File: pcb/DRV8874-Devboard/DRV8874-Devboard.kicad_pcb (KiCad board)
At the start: 4 copper layers, 65 x 67 mm, 40 parts, among them J1 Conn_01x04_Pin, J2 Screw_Terminal_01x02, J3 Conn_01x03_Pin, J4 Conn_01x03_Pin, J5 Conn_01x04_Pin, J6 Conn_01x03_Pin, J7 Conn_01x03_Pin, J8 Conn_01x04_Pin, J9 Conn_01x03_Pin, U1 DRV8874, U2 BL9342, U4 SN65HVD230, U5 TPS16630PWPR, U7 TinyThinker_J1

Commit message: started working on CAN
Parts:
- moved U4 34.4 mm to (141.0, 92.5), turned to -90 degrees
- moved R3 27.5 mm to (141.5, 98.5)
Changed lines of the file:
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@@
 	(footprint "Resistor_SMD:R_0402_1005Metric"
 		(layer "F.Cu")
-		(at 164.03 82.8)
+		(at 141.5 98.5)
 		(descr "Resistor SMD 0402 (1005 Metric), square (rectangular) end terminal, IPC-7351 nominal, (Body size source: IPC-SM-782 page 72, https://www.pcb-3d.com/wordpress/wp-content/uploads/ipc-sm-782a_amendment_1_and_2.pdf), generated with kicad-footprint-generator")
 		(tags "resistor")
@@
 	(footprint "Package_SO:SOIC-8_3.9x4.9mm_P1.27mm"
 		(layer "F.Cu")
-		(at 163.15 66.135)
+		(at 141 92.5 -90)
 		(descr "SOIC, 8 Pin (JEDEC MS-012AA, https://www.analog.com/media/en/package-pcb-resources/package/pkg_pdf/soic_narrow-r/r_8.pdf), generated with kicad-footprint-generator ipc_gullwing_generator.py")
 		(tags "SOIC SO")
 		(property "Reference" "U4"
-			(at 0 -3.4 0)
+			(at 0 -4 90)
 			(layer "F.SilkS")
 			(effects
@@
 		)
 		(property "Value" "SN65HVD230"
-			(at 0 3.4 0)
+			(at 0 3.4 90)
 			(layer "F.Fab")
 			(effects
@@
 		)
 		(property "Datasheet" "http://www.ti.com/lit/ds/symlink/sn65hvd230.pdf"
-			(at 0 0 0)
+			(at 0 0 90)
 			(layer "F.Fab")
 			(hide yes)
@@
 		)
 		(property "Description" "CAN Bus Transceivers, 3.3V, 1Mbps, Low-Power capabilities, SOIC-8"
-			(at 0 0 0)
+			(at 0 0 90)
 			(layer "F.Fab")
 			(hide yes)
@@
 		)
 		(property "Sim.Device" ""
-			(at 0 0 0)
+			(at 0 0 270)
 			(unlocked yes)
 			(layer "F.Fab")
@@
 		)
 		(property "Sim.Pins" ""
-			(at 0 0 0)
+			(at 0 0 270)
 			(unlocked yes)
 			(layer "F.Fab")
@@
 		)
 		(property "Sim.Type" ""
-			(at 0 0 0)
+			(at 0 0 270)
 			(unlocked yes)
 			(layer "F.Fab")
@@
 		(attr smd)
 		(fp_line
-			(start -2.06 -2.56)
-			(end 2.06 -2.56)
+			(start -2.06 2.56)
+			(end -2.06 2.465)
 			(stroke
 				(width 0.12)
@@
 		)
 		(fp_line
-			(start -2.06 -2.465)
-			(end -2.06 -2.56)
+			(start 2.06 2.56)
+			(end -2.06 2.56)
 			(stroke
 				(width 0.12)
@@
 		)
 		(fp_line
-			(start -2.06 2.56)
-			(end -2.06 2.465)
+			(start 2.06 2.465)
+			(end 2.06 2.56)
 			(stroke
 				(width 0.12)
@@
 		)
 		(fp_line
-			(start 2.06 -2.56)
-			(end 2.06 -2.465)
+			(start -2.06 -2.465)
+			(end -2.06 -2.56)
 			(stroke
 				(width 0.12)
@@
 		)
 		(fp_line
-			(start 2.06 2.465)
-			(end 2.06 2.56)
+			(start -2.06 -2.56)
+			(end 2.06 -2.56)
 			(stroke
 				(width 0.12)
@@
 		)
 		(fp_line
-			(start 2.06 2.56)
-			(end -2.06 2.56)
+			(start 2.06 -2.56)
+			(end 2.06 -2.465)
 			(stroke
 				(width 0.12)
@@
 		)
 		(fp_line
-			(start -3.7 -2.46)
-			(end -2.2 -2.46)
+			(start -2.2 2.7)
+			(end -2.2 2.46)
 			(stroke
 				(width 0.05)
@@
 		)
 		(fp_line
-			(start -3.7 2.46)
-			(end -3.7 -2.46)
+			(start 2.2 2.7)
+			(end -2.2 2.7)
 			(stroke
 				(width 0.05)
@@
 		)
 		(fp_line
-			(start -2.2 -2.7)
-			(end 2.2 -2.7)
+			(start -3.7 2.46)
+			(end -3.7 -2.46)
 			(stroke
 				(width 0.05)
@@
 		)
 		(fp_line
-			(start -2.2 -2.46)
-			(end -2.2 -2.7)
+			(start -2.2 2.46)
+			(end -3.7 2.46)
 			(stroke
 				(width 0.05)
@@
 		)
 		(fp_line
-			(start -2.2 2.46)
-			(end -3.7 2.46)
+			(start 2.2 2.46)
+			(end 2.2 2.7)
 			(stroke
 				(width 0.05)
@@
 		)
 		(fp_line
-			(start -2.2 2.7)
-			(end -2.2 2.46)
+			(start 3.7 2.46)
+			(end 2.2 2.46)
 			(stroke
 				(width 0.05)
@@
 		)
 		(fp_line
-			(start 2.2 -2.7)
-			(end 2.2 -2.46)
+			(start -3.7 -2.46)
+			(end -2.2 -2.46)
 			(stroke
 				(width 0.05)
@@
 		)
 		(fp_line
-			(start 2.2 -2.46)
-			(end 3.7 -2.46)
+			(start -2.2 -2.46)
+			(end -2.2 -2.7)
 			(stroke
 				(width 0.05)
@@
 		)
 		(fp_line
-			(start 2.2 2.46)
-			(end 2.2 2.7)
+			(start 2.2 -2.46)
+			(end 3.7 -2.46)
 			(stroke
 				(width 0.05)
@@
 		)
 		(fp_line
-			(start 2.2 2.7)
-			(end -2.2 2.7)
+			(start 3.7 -2.46)
+			(end 3.7 2.46)
 			(stroke
 				(width 0.05)
@@
 		)
 		(fp_line
-			(start 3.7 -2.46)
-			(end 3.7 2.46)
+			(start -2.2 -2.7)
+			(end 2.2 -2.7)
 			(stroke
 				(width 0.05)
@@
 		)
 		(fp_line
-			(start 3.7 2.46)
-			(end 2.2 2.46)
+			(start 2.2 -2.7)
+			(end 2.2 -2.46)
 			(stroke
 				(width 0.05)
@@
 		)
 		(fp_text user "${REFERENCE}"
-			(at 0 0 90)
+			(at 0 0 0)
 			(layer "F.Fab")
 			(effects
@@
 		)
 		(pad "1" smd roundrect
-			(at -2.475 -1.905)
+			(at -2.475 -1.905 270)
 			(size 1.95 0.6)
 			(layers "F.Cu" "F.Mask" "F.Paste")
@@
 		)
 		(pad "2" smd roundrect
-			(at -2.475 -0.635)
+			(at -2.475 -0.635 270)
 			(size 1.95 0.6)
 			(layers "F.Cu" "F.Mask" "F.Paste")
@@
 		)
 		(pad "3" smd roundrect
-			(at -2.475 0.635)
+			(at -2.475 0.635 270)
 			(size 1.95 0.6)
 			(layers "F.Cu" "F.Mask" "F.Paste")
@@
 		)
 		(pad "4" smd roundrect
-			(at -2.475 1.905)
+			(at -2.475 1.905 270)
 			(size 1.95 0.6)
 			(layers "F.Cu" "F.Mask" "F.Paste")
@@
 		)
 		(pad "5" smd roundrect
-			(at 2.475 1.905)
+			(at 2.475 1.905 270)
 			(size 1.95 0.6)
 			(layers "F.Cu" "F.Mask" "F.Paste")
@@
 		)
 		(pad "6" smd roundrect
-			(at 2.475 0.635)
+			(at 2.475 0.635 270)
 			(size 1.95 0.6)
 			(layers "F.Cu" "F.Mask" "F.Paste")
@@
 		)
 		(pad "7" smd roundrect
-			(at 2.475 -0.635)
+			(at 2.475 -0.635 270)
 			(size 1.95 0.6)
 			(layers "F.Cu" "F.Mask" "F.Paste")
@@
 		)
 		(pad "8" smd roundrect
-			(at 2.475 -1.905)
+			(at 2.475 -1.905 270)
 			(size 1.95 0.6)
 			(layers "F.Cu" "F.Mask" "F.Paste")

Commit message: Started working on layout
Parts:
- added C6: 330uF, Capacitor_SMD:CP_Elec_10x10.5, F.Cu at (187.2, 81.4)
- added C7: 22nF, Capacitor_SMD:C_0603_1608Metric, F.Cu at (181.8, 88.7)
- added C8: 100nF, Capacitor_SMD:C_0402_1005Metric, F.Cu at (195.8, 76.3)
- added C9: 100nF, Capacitor_SMD:C_0402_1005Metric, F.Cu at (195.8, 78.3)
- added J10: Conn_01x06_Pin, Connector_PinHeader_2.54mm:PinHeader_1x06_P2.54mm_Vertical, F.Cu at (109.0, 70.7)
- added J11: Conn_01x04_Pin, Connector_PinHeader_2.54mm:PinHeader_1x04_P2.54mm_Vertical, F.Cu at (177.5, 77.7)
- added J12: Conn_01x03_Pin, Connector_PinHeader_2.54mm:PinHeader_1x03_P2.54mm_Vertical, F.Cu at (186.1, 89.7)
- added R16: 15k, Resistor_SMD:R_0603_1608Metric, F.Cu at (181.8, 91.2)
- added R17: 75k, Resistor_SMD:R_0603_1608Metric, F.Cu at (181.8, 93.7)
- added R18: 20k, Resistor_SMD:R_0603_1608Metric, F.Cu at (181.8, 96.2)
- added R19: 2k2, Resistor_SMD:R_0402_1005Metric, F.Cu at (194.2, 95.0)
- added R20: 10k, Resistor_SMD:R_0805_2012Metric, F.Cu at (190.6, 95.5)
- added U3: DRV8874, Package_SO:HTSSOP-16-1EP_4.4x5mm_P0.65mm_EP3.4x5mm_Mask2.46x2.31mm, F.Cu at (135.1, 72.5)
- R10, R7: footprint PCM_JLCPCB:R_0603 -> Resistor_SMD:R_0603_1608Metric
- U1: footprint Package_SO:HTSSOP-16-1EP_4.4x5mm_P0.65mm_EP3.4x5mm_Mask2.66x2.46mm -> Package_SO:HTSSOP-16-1EP_4.4x5mm_P0.65mm_EP3.4x5mm_Mask2.46x2.31mm
- U7: moved to B.Cu
- moved J9 70.9 mm to (125.0, 51.5), turned to -90 degrees
- moved J8 66.1 mm to (127.6, 47.5), turned to -90 degrees
- moved R2 65.8 mm to (122.0, 93.5)
- moved R15 65.7 mm to (128.0, 52.0), turned to -90 degrees
- moved C1 55.1 mm to (133.2, 53.3), turned to 180 degrees
- moved R13 54.7 mm to (130.0, 57.8), turned to -90 degrees
- moved R14 53.8 mm to (130.0, 61.3), turned to -90 degrees
- moved U5 52.9 mm to (136.5, 97.5), turned to 90 degrees
- moved C13 52.6 mm to (187.5, 109.2), turned to 90 degrees
- moved J7 50.2 mm to (111.5, 104.5), turned to 90 degrees
- moved R6 49.4 mm to (137.0, 89.5), turned to -90 degrees
- moved R11 46.7 mm to (185.5, 109.2), turned to -90 degrees
- moved J6 43.1 mm to (121.0, 85.4)
- moved J4 42.8 mm to (111.4, 96.5), turned to 90 degrees
- moved R12 42.4 mm to (185.5, 112.7), turned to 90 degrees
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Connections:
- net /BL9342_EN renamed /BL_EN
- net /PMODE_A renamed /A_PMODE
- net Net-(D2-K) renamed /BL_SW
- net Net-(J4-Pin_2) renamed /CAN_TERM
- net Net-(J6-Pin_2) renamed /CAN_RS
- net Net-(J6-Pin_3) renamed /CAN_RS_R
- net Net-(J9-Pin_1) renamed /A_IMODE_R
- net Net-(J9-Pin_2) renamed /A_IMODE
- net Net-(U1-CPH) renamed /A_CPH
- net Net-(U1-CPL) renamed /A_CPL
- net Net-(U1-VCP) renamed /A_VCP
- net Net-(U1-VREF) renamed /A_VREF
- net Net-(U1-nFAULT) renamed /A_nFault
- net Net-(U2-BST) renamed /BL_BST
- net Net-(U2-FB) renamed /BL_FB
- net Net-(U5-*FLT) renamed /TPS_FLT
- net Net-(U5-DVDT) renamed /TPS_DVDT
- net Net-(U5-ILIM) renamed /TPS_ILIM
- net Net-(U5-IMON) renamed /TPS_MON
- net Net-(U5-OVP) renamed /TPS_OVP
- net Net-(U5-UVLO) renamed /TPS_UVLO
- C12 pad 1: Net-(U2-VIN) -> +BATT_PROT
- R1 pad 1: Net-(U1-IPROPI) -> /A_IPROPI
- U1 pad 1: unconnected-(U1-EN/IN1-Pad1) -> /A_IN1
- U1 pad 10: /Phase_A- -> /A_OUT-
- U1 pad 2: unconnected-(U1-PH/IN2-Pad2) -> /A_IN2
- U1 pad 6: Net-(U1-IPROPI) -> /A_IPROPI
- U1 pad 8: /Phase_A+ -> /A_OUT+
- U2 pad 5: Net-(U2-VIN) -> +BATT_PROT
- U7 pad 1: unconnected-(U7A-+5V_EXT-Pad1) -> +5V
- U7 pad 10: unconnected-(U7A-GND-Pad10) -> GND
- U7 pad 11: unconnected-(U7A-GND-Pad11) -> GND
- U7 pad 13: unconnected-(U7A-+3.3V-Pad13) -> +3.3V
- U7 pad 14: unconnected-(U7A-GND-Pad14) -> GND
- U7 pad 15: unconnected-(U7A-GND-Pad15) -> GND
- U7 pad 16: unconnected-(U7A-+3.3V-Pad16) -> +3.3V
- U7 pad 17: unconnected-(U7A-ADC1_IN9-Pad17) -> /A_IPROPI
- U7 pad 18: unconnected-(U7A-GND-Pad18) -> GND
- U7 pad 19: unconnected-(U7A-GND-Pad19) -> GND
- U7 pad 2: unconnected-(U7A-GND-Pad2) -> GND
- U7 pad 21: unconnected-(U7A-ADC1_IN15-Pad21) -> /B_IPROPI
- U7 pad 22: unconnected-(U7A-GND-Pad22) -> GND
- U7 pad 23: unconnected-(U7A-GND-Pad23) -> GND
- U7 pad 25: unconnected-(U7A-+3.3V-Pad25) -> +3.3V
- U7 pad 26: unconnected-(U7A-GND-Pad26) -> GND
- U7 pad 27: unconnected-(U7A-GND-Pad27) -> GND
- U7 pad 28: unconnected-(U7A-+3.3V-Pad28) -> +3.3V
- U7 pad 30: unconnected-(U7A-GND-Pad30) -> GND
- U7 pad 31: unconnected-(U7A-GND-Pad31) -> GND
- U7 pad 34: unconnected-(U7A-GND-Pad34) -> GND
- U7 pad 35: unconnected-(U7A-GND-Pad35) -> GND
- U7 pad 37: unconnected-(U7A-+3.3V-Pad37) -> +3.3V
- U7 pad 38: unconnected-(U7A-GND-Pad38) -> GND
- U7 pad 39: unconnected-(U7A-GND-Pad39) -> GND
- U7 pad 4: unconnected-(U7A-GND-Pad4) -> GND
- U7 pad 51: unconnected-(U7B-SPI1_NSS-Pad51) -> /SPI1_NSS
- U7 pad 53: unconnected-(U7B-SPI1_SCK-Pad53) -> /SPI1_SCK
- U7 pad 55: unconnected-(U7B-SPI1_MISO-Pad55) -> /SPI1_MISO
- U7 pad 57: unconnected-(U7B-SPI1_MOSI-Pad57) -> /SPI1_MOSI
- U7 pad 6: unconnected-(U7A-GND-Pad6) -> GND
- U7 pad 7: unconnected-(U7A-GND-Pad7) -> GND
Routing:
- net /CAN1_TX: track 0.00 -> 13.3 mm
- net /CAN_H: track 0.00 -> 12.3 mm
- net /CAN1_RX: track 0.00 -> 9.59 mm
- net /CAN_RS: track 0.00 -> 7.77 mm
- net /SPI1_MOSI: track 0.00 -> 7.77 mm
- net /SPI1_MISO: track 0.00 -> 7.77 mm
- net /SPI1_SCK: track 0.00 -> 7.77 mm
- net /SPI1_NSS: track 0.00 -> 7.77 mm
- net /CAN_L: track 0.00 -> 6.09 mm
- net /TPS_MON: track 0.00 -> 5.44 mm
- net +BATT_RAW: track 0.00 -> 5.02 mm
- net /TPS_OVP: track 0.00 -> 4.90 mm
- net /I2C1_SDA: track 0.00 -> 4.80 mm
- net /I2C1_SCL: track 0.00 -> 4.80 mm
- net /TPS_UVLO: track 0.00 -> 4.73 mm
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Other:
- board text added: "3V3"
- board text added: "CAN1"
- board text added: "GND"
- board text added: "HI"
- board text added: "I2C1"
- board text added: "LO"
- board text added: "MISO"
- board text added: "MOSI"
- board text added: "NSS"
- board text added: "SCK"
- board text added: "SCL"
- board text added: "SDA"
- board text added: "SPI1"

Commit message: checkpoint
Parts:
- moved J1 76.2 mm to (143.5, 59.9), turned to 0 degrees
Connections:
- J1 pad 1: /Phase_B- -> /B_OUT-
- J1 pad 2: /Phase_A- -> /A_OUT-
- J1 pad 3: /Phase_B+ -> /B_OUT+
- J1 pad 4: /Phase_A+ -> /A_OUT+

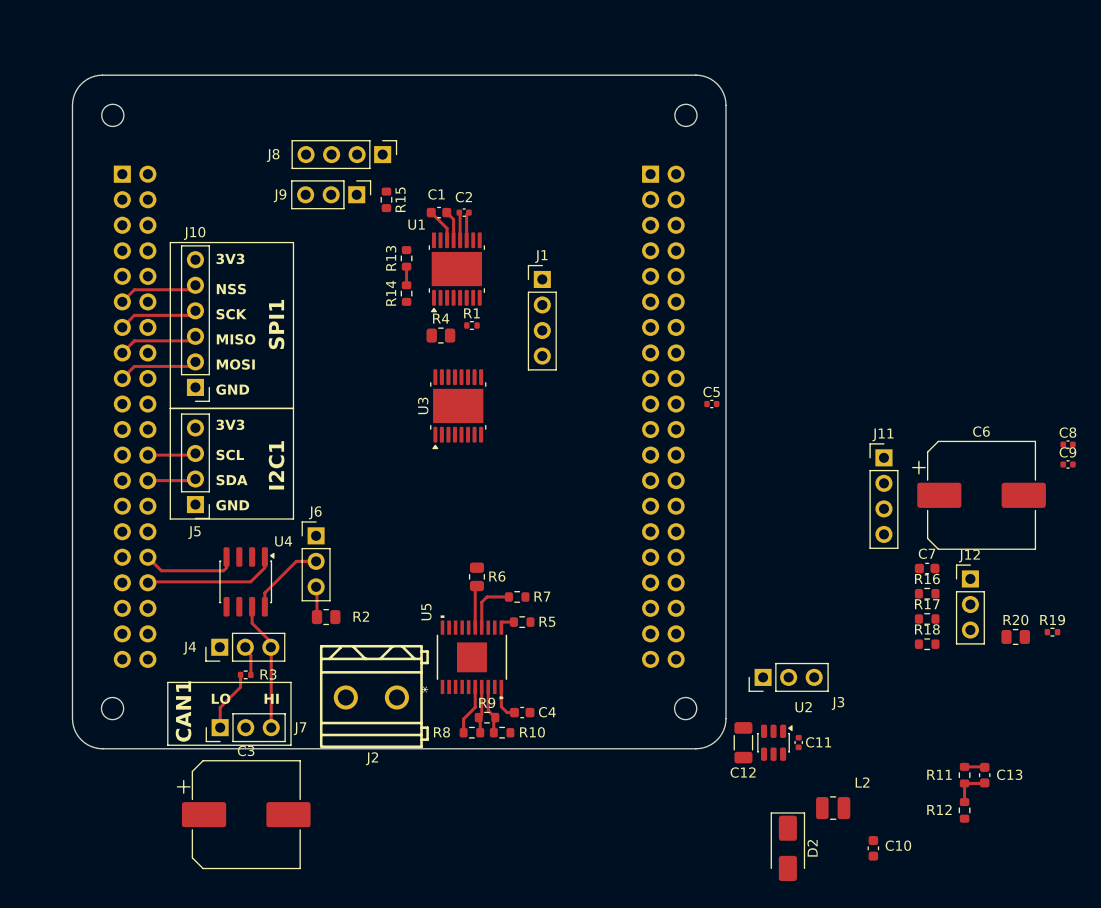
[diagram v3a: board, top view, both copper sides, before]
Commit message: minor component routing
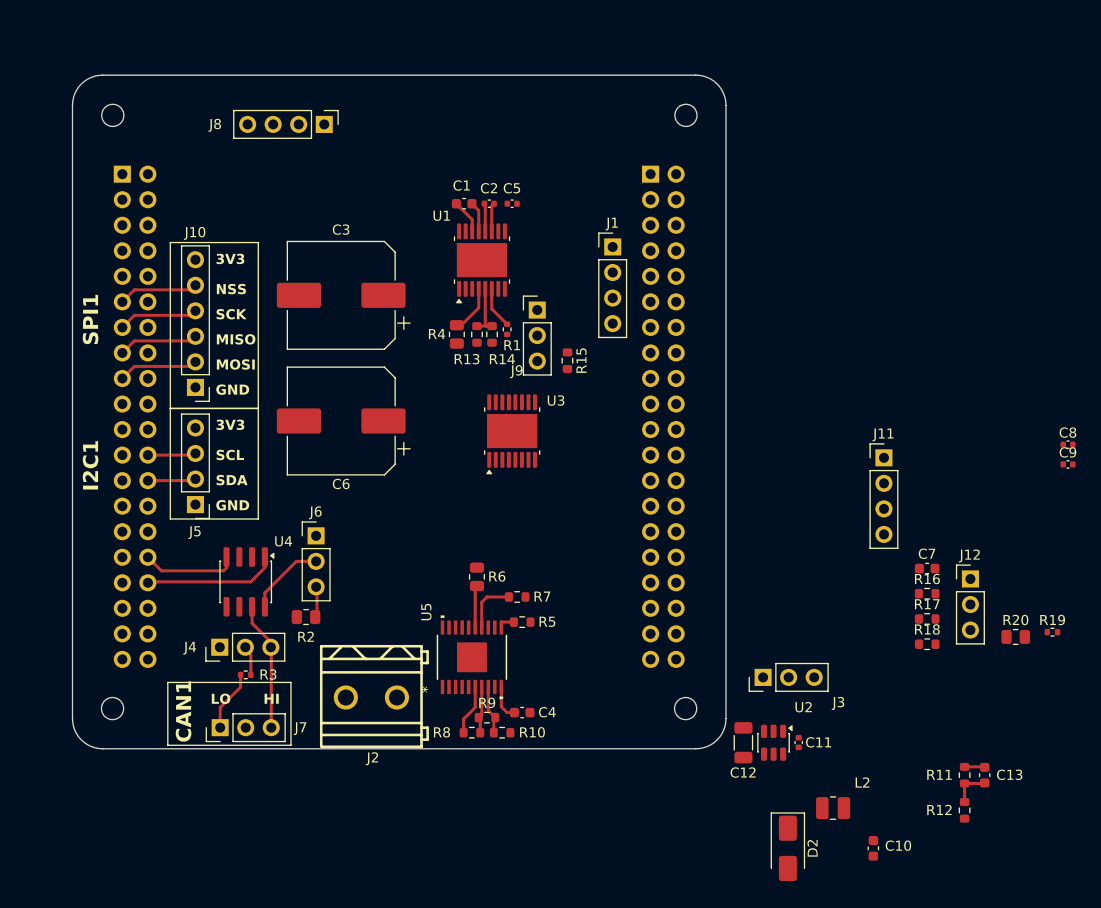
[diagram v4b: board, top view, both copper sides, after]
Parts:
- moved C6 64.1 mm to (123.5, 74.0), turned to 180 degrees
- moved C3 52.5 mm to (123.5, 61.5), turned to 180 degrees
- moved C5 28.1 mm to (140.5, 52.4)
- moved R15 24.1 mm to (146.0, 68.0)
- moved J9 21.3 mm to (143.0, 63.0), turned to 0 degrees
- moved R13 10.3 mm to (137.0, 65.4), turned to 90 degrees
- moved R14 9.42 mm to (138.5, 65.4)
- moved J1 7.71 mm to (150.5, 56.7)
- moved J8 6.54 mm to (121.8, 44.5)
- moved U3 5.92 mm to (140.5, 75.0)
- moved R1 3.52 mm to (140.0, 64.9), turned to -90 degrees
- moved C1 2.65 mm to (135.7, 52.4)
- moved C2 2.65 mm to (138.2, 52.4)
- moved U1 2.65 mm to (137.5, 58.0)
- moved R2 2.00 mm to (120.0, 93.5), turned to 180 degrees
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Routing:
- net /A_nFault: track 0.00 -> 4.78 mm
- net /A_IPROPI: track 0.00 -> 4.14 mm
- net /A_VREF: track 1.85 -> 5.27 mm

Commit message: removed jumper to switch PMODE since IN/I N seems to have the most benefits
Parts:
- removed J11, J8: Conn_01x04_Pin, Connector_PinHeader_2.54mm:PinHeader_1x04_P2.54mm_Vertical
- moved U3 4.91 mm to (143.5, 78.9)
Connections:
- U1 pad 16: /A_PMODE -> +3.3V
- U3 pad 16: /B_PMODE -> +3.3V
